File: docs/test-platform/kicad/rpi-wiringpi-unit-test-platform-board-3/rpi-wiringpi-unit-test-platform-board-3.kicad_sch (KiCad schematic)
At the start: 19 parts, among them J1 JST_IN_PWR, J2 JST_IN_SIG, J3 JST_OUT_PWR, J4 JST_OUT_SW, J5 JST_OUT_COIL, J6 JST_IO_A4_7, J7 JST_IO_B0_3, J8 JST_IO_B4_7, SW1 DIP_SW_x3, U1 MCP23017_0x20, U2 MCP23017_0x21

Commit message: Updates
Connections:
- net GPIO19: now also SW1.3; no longer SW1.5
- net GPIO27: now also SW1.2; no longer SW1.3
- net LED_G_A: now also SW1.6; no longer SW1.2
- net LED_R_A: now also SW1.5; no longer SW1.4
- net LED_Y_A: now also SW1.4; no longer SW1.6
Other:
- moved on the sheet: D1, J1, J2, J3, J4, J5, J6, J7, J8

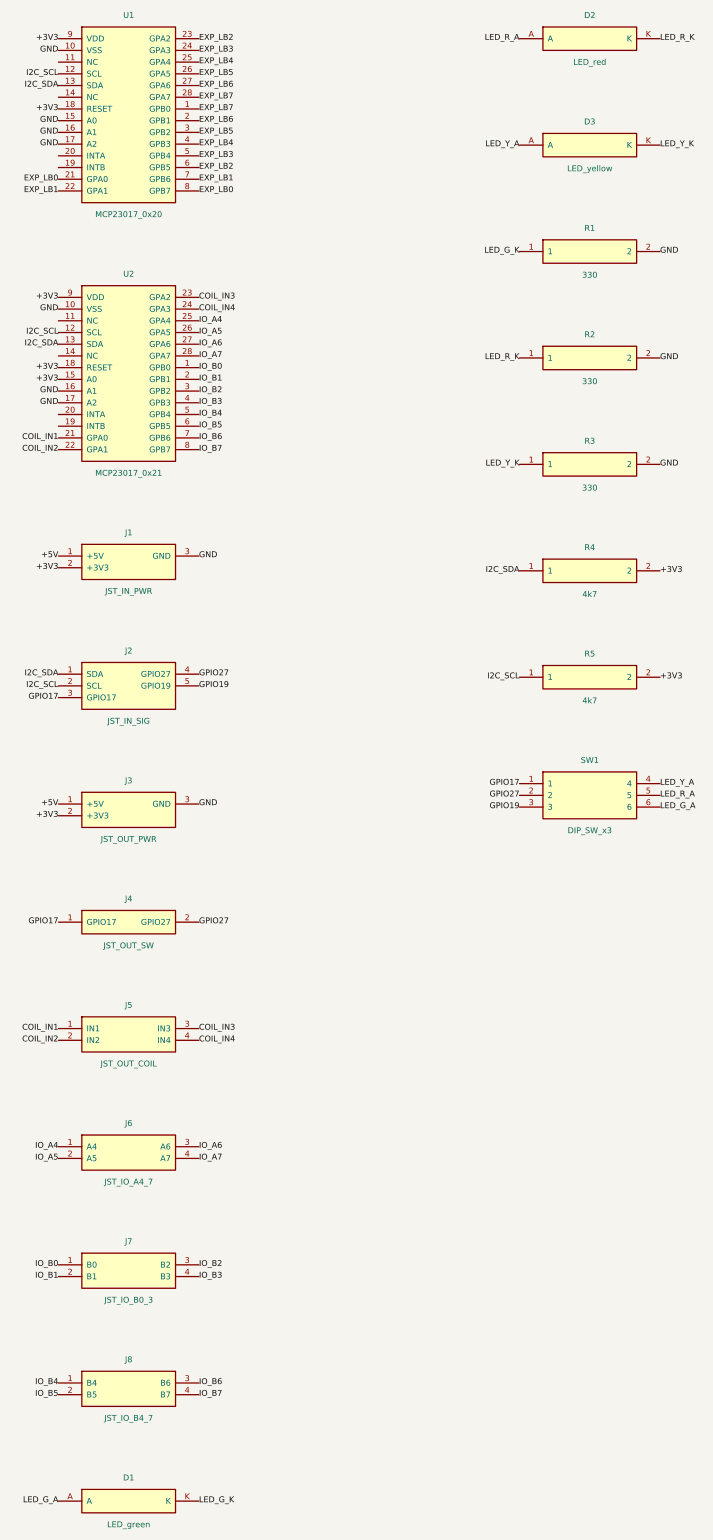
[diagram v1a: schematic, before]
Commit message: Completely finished unit test board #3 (production ordered)
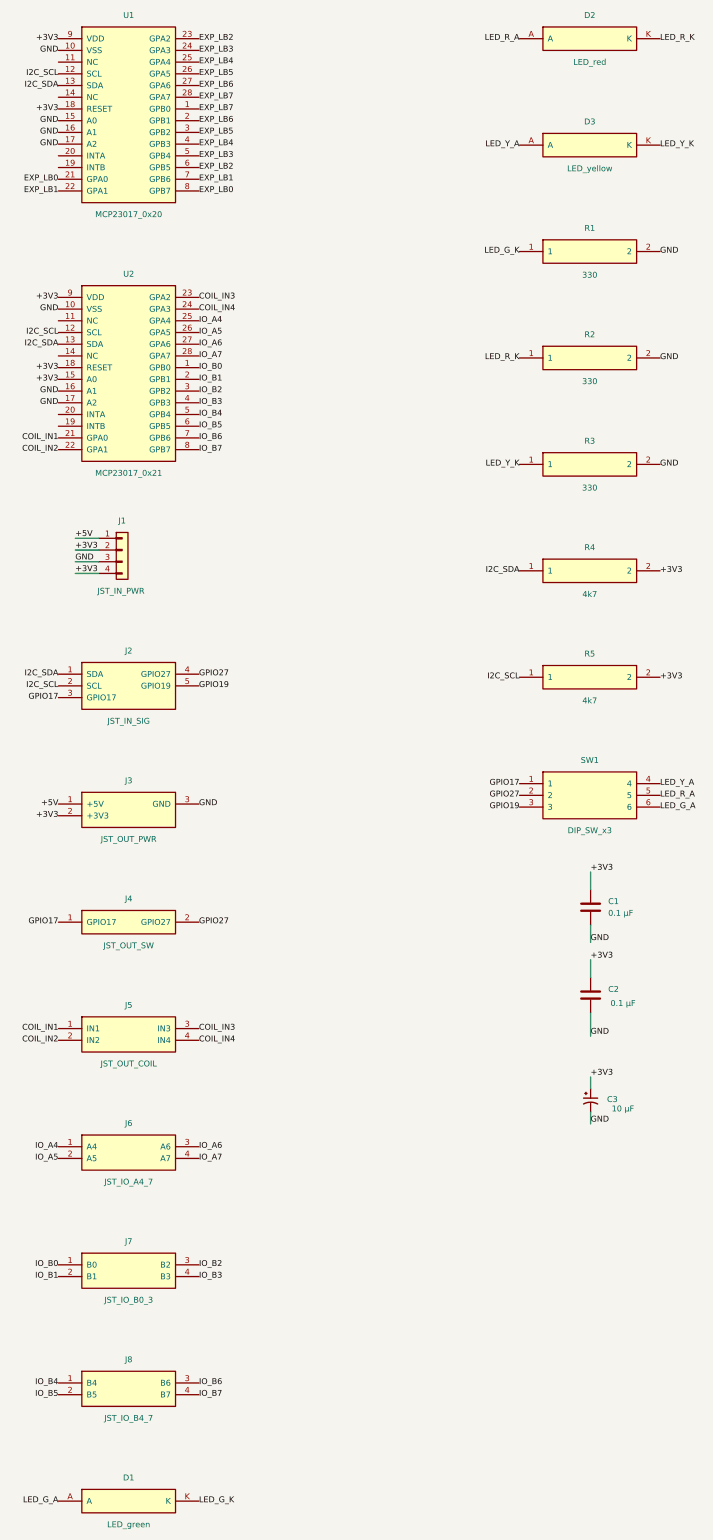
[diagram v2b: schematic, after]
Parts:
- added C1, C2: 0.1 µF, Capacitor_THT:C_Disc_D5.0mm_W2.5mm_P2.50mm, symbol Device:C
- added C3: 10 µF, Capacitor_THT:CP_Radial_D5.0mm_P2.50mm, symbol Device:C_Polarized_Small_US
- J1: symbol rpi-wiringpi-unit-test-platform-board-3:J1 -> Connector_Generic:Conn_01x04
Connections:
- net GND: now also C1.2, C2.2, C3.2
- net +3V3: no longer names the net of J1.2 (Pin_2), J3.2 (+3V3), R4.2, R5.2, U1.18 (RESET), U1.9 (VDD), U2.15 (A0), U2.18 (RESET), U2.9 (VDD)
- net +3V3: now also J1.4 (Pin_4), C1.1, C2.1, C3.1

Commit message: Finalize board 3
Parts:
- D1: value LED_green -> LED_G
- D2: value LED_red -> LED_R
- D3: value LED_yellow -> LED_Y
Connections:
- net +3V3: now reaches C1.1, C2.1, C3.1, J1.2 (Pin_2), J1.4 (Pin_4), J3.2 (+3V3), R4.2, R5.2, U1.18 (RESET), U1.9 (VDD), U2.15 (A0), U2.18 (RESET), U2.9 (VDD)
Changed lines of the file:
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@@
 	(wire
 		(pts
-			(xy 58.42 143.51) (xy 63.5 143.51)
+			(xy 50.8 143.51) (xy 63.5 143.51)
 		)
 		(stroke
@@
 	)
 	(label "+3V3"
+		(at 58.42 143.51 0)
+		(effects
+			(font
+				(size 1.27 1.27)
+			)
+			(justify left bottom)
+		)
+	)
+	(label "+3V3"
 		(at 170.18 227.33 0)
 		(effects
@@
 			)
 			(justify left)
-		)
-	)
-	(label "+3V3"
-		(at 58.42 143.51 0)
-		(effects
-			(font
-				(size 1.27 1.27)
-			)
-			(justify left bottom)
 		)
 	)
@@
 			)
 		)
-		(property "Value" "LED_red"
+		(property "Value" "LED_R"
 			(at 170 32.62 0)
 			(show_name no)
@@
 	)
 	(symbol
+		(lib_id "power:+3V3")
+		(at 50.8 143.51 0)
+		(unit 1)
+		(body_style 1)
+		(exclude_from_sim no)
+		(in_bom yes)
+		(on_board yes)
+		(in_pos_files yes)
+		(dnp no)
+		(property "Reference" "#PWR01"
+			(at 50.8 147.32 0)
+			(hide yes)
+			(show_name no)
+			(do_not_autoplace no)
+			(effects
+				(font
+					(size 1.27 1.27)
+				)
+			)
+		)
+		(property "Value" "+3V3"
+			(at 50.038 137.922 0)
+			(show_name no)
+			(do_not_autoplace no)
+			(effects
+				(font
+					(size 1.27 1.27)
+				)
+			)
+		)
+		(property "Footprint" ""
+			(at 50.8 143.51 0)
+			(hide yes)
+			(show_name no)
+			(do_not_autoplace no)
+			(effects
+				(font
+					(size 1.27 1.27)
+				)
+			)
+		)
+		(property "Datasheet" ""
+			(at 50.8 143.51 0)
+			(hide yes)
+			(show_name no)
+			(do_not_autoplace no)
+			(effects
+				(font
+					(size 1.27 1.27)
+				)
+			)
+		)
+		(property "Description" "Power symbol creates a global label with name \"+3V3\""
+			(at 50.8 143.51 0)
+			(hide yes)
+			(show_name no)
+			(do_not_autoplace no)
+			(effects
+				(font
+					(size 1.27 1.27)
+				)
+			)
+		)
+		(pin "1"
+		)
+		(instances
+			(project "rpi-wiringpi-unit-test-platform-board-3"
+				(path "/d32517a0-ba1d-5be2-8d0f-f7fb5839afe5"
+					(reference "#PWR01")
+					(unit 1)
+				)
+			)
+		)
+	)
+	(symbol
 		(lib_id "Device:C_Polarized_Small_US")
 		(at 170.18 257.81 0)
@@
 			)
 		)
-		(property "Value" "LED_green"
+		(property "Value" "LED_G"
 			(at 70 349.78 0)
 			(show_name no)
@@
 			)
 		)
-		(property "Value" "LED_yellow"
+		(property "Value" "LED_Y"
 			(at 170 55.7 0)
 			(show_name no)
